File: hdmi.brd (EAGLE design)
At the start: 160 x 100 mm, 143 parts, among them IC1 FT2232HQ, U0 6SLX45CSG324, U1 MT41J64M16, U2 TPD12S016RKTR, U3 TPD12S016RKTR, U4 TPD12S016RKTR, U5 MNR18, U6 MNR18, U8 20Mhz

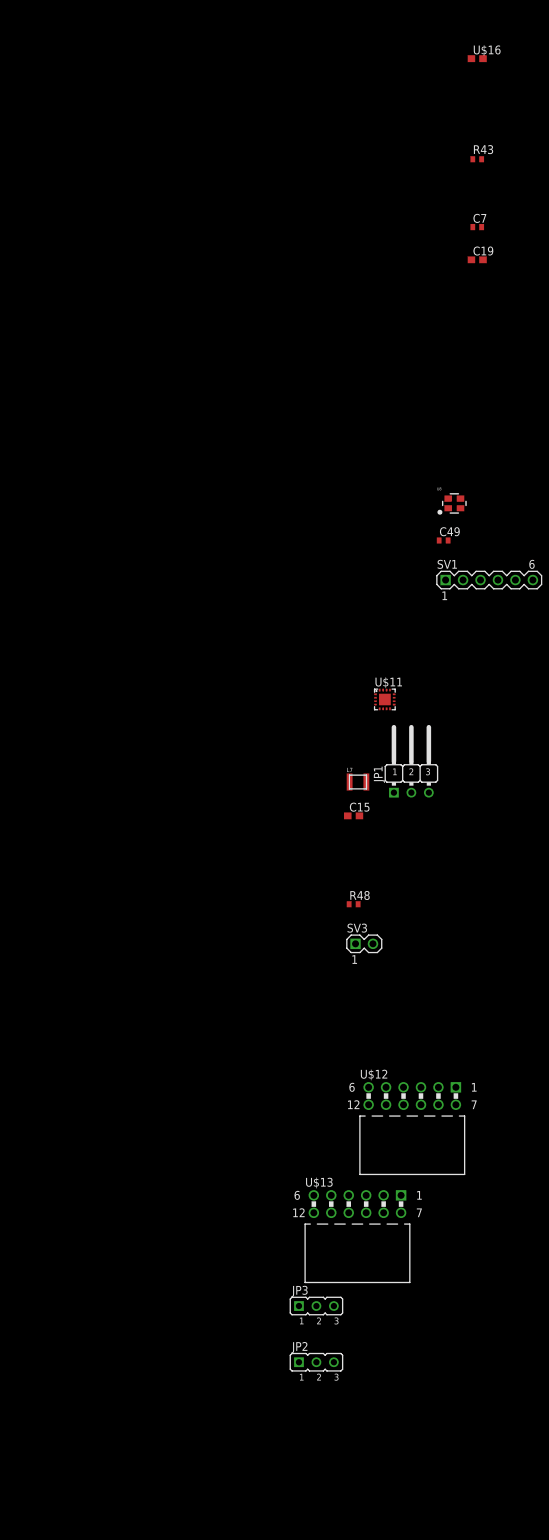
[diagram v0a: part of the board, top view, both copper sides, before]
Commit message: +Toslink
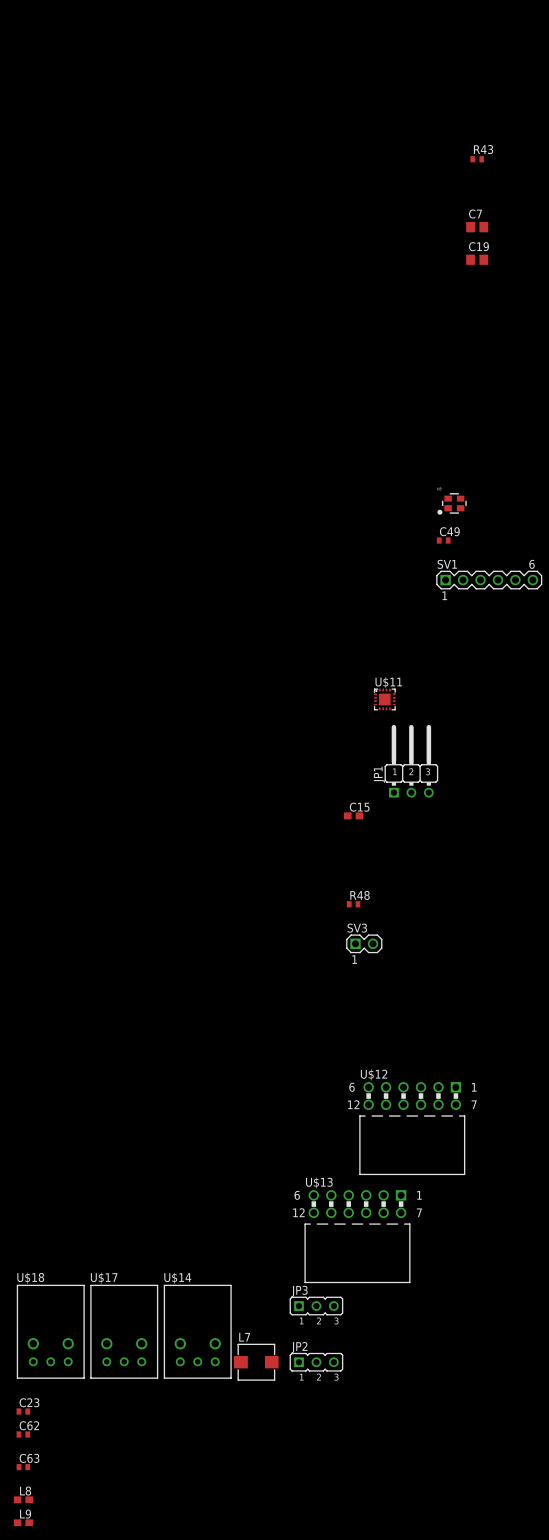
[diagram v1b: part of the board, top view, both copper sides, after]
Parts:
- removed U$16: 3A, prj-hdmi:0603
- added C23, C62, C63: 0.1u, prj-hdmi:0402
- added L8, L9: 47u, prj-hdmi:0603
- added U$14: PLT133-T10W, prj-hdmi:PLR135-T10_PLT133-T10W
- added U$17, U$18: PLR135-T10, prj-hdmi:PLR135-T10_PLT133-T10W
- C19: value 10u -> 47u; device prj-hdmi:0603 -> prj-hdmi:0805
- C7: value 10u -> 47u; device prj-hdmi:0402 -> prj-hdmi:0805
- L7: value 3.3u, 4A -> 3.3u, 5A; device prj-hdmi:1008 -> prj-hdmi:SRP5030T
- moved L7 85.7 mm to (-180.7, -914.0)
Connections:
- removed net N$29: C19.1, R48.2, U$11.11, U$11.2, U$11.3, U$16.2
- new net N$36: C23.1, L8.2, U$18.1
- new net N$4: C62.1, L9.2, U$17.1
- new net TOS_IN0: U$18.3
- new net TOS_IN1: U$17.3
- new net TOS_OUT0: U$14.3
- net +3V3: now also C57.1, C63.1, L8.1, L9.1, U$14.2; no longer C57.2
- net CENTER: now also C19.1, R48.2, U$11.11, U$11.2, U$11.3; no longer U$16.1
- net GND: now also C23.2, C57.2, C62.2, C63.2, U$14.1, U$17.2, U$18.2; no longer C57.1

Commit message: +Toslink connections
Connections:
- new net N$19: R48.1, U$11.8
- net TOS_IN0: now also U0.A2
- net TOS_IN1: now also U0.T18
- net TOS_OUT0: now also U0.V6
- net USB_5V_DISABLE: no longer R48.1, U$11.8
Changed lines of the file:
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@@
 <contactref element="U$10" pad="3"/>
 <contactref element="R44" pad="2"/>
-<contactref element="U$11" pad="8"/>
-<contactref element="R48" pad="1"/>
-<wire x1="-161.2766" y1="-818.9098" x2="-167.2232" y2="-847.344" width="0" layer="19" extent="1-1"/>
-<wire x1="-147.94" y1="-660.4" x2="-161.2766" y2="-818.9098" width="0" layer="19" extent="1-1"/>
 <wire x1="-148.59" y1="-655.1" x2="-147.94" y2="-660.4" width="0" layer="19" extent="1-1"/>
 </signal>
@@
 <signal name="TOS_IN0">
 <contactref element="U$18" pad="3"/>
+<contactref element="U0" pad="A2"/>
+<wire x1="-45.4" y1="16" x2="-213.1822" y2="-913.9312" width="0" layer="19" extent="1-1"/>
 </signal>
 <signal name="TOS_IN1">
 <contactref element="U$17" pad="3"/>
+<contactref element="U0" pad="T18"/>
+<wire x1="-32.6" y1="4" x2="-202.4888" y2="-913.9312" width="0" layer="19" extent="1-1"/>
 </signal>
 <signal name="TOS_OUT0">
 <contactref element="U$14" pad="3"/>
+<contactref element="U0" pad="V6"/>
+<wire x1="-42.2" y1="2.4" x2="-191.7954" y2="-913.9312" width="0" layer="19" extent="1-1"/>
+</signal>
+<signal name="N$19">
+<contactref element="U$11" pad="8"/>
+<contactref element="R48" pad="1"/>
+<wire x1="-161.2766" y1="-818.9098" x2="-167.2232" y2="-847.344" width="0" layer="19" extent="1-1"/>
 </signal>
 </signals>

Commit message: +Schematic notes
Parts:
- removed R48: 10k, prj-hdmi:0402
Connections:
- removed net N$19: R48.1, U$11.8
- net CENTER: no longer R48.2
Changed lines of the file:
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@@
 <layers>
 <layer number="1" name="Top" color="4" fill="1" visible="yes" active="yes"/>
-<layer number="2" name="Ground" color="1" fill="3" visible="no" active="no"/>
+<layer number="2" name="Ground" color="1" fill="3" visible="no" active="yes"/>
 <layer number="3" name="Route3" color="4" fill="3" visible="no" active="no"/>
 <layer number="4" name="Route4" color="1" fill="4" visible="no" active="no"/>
@@
 <layer number="13" name="Route13" color="4" fill="5" visible="no" active="no"/>
 <layer number="14" name="Route14" color="1" fill="6" visible="no" active="no"/>
-<layer number="15" name="VCC" color="4" fill="6" visible="no" active="no"/>
+<layer number="15" name="VCC" color="4" fill="6" visible="no" active="yes"/>
 <layer number="16" name="Bottom" color="1" fill="1" visible="yes" active="yes"/>
 <layer number="17" name="Pads" color="2" fill="1" visible="yes" active="yes"/>
@@
 </class>
 </classes>
-<designrules name="default">
+<designrules name="default *">
 <description language="de">&lt;b&gt;EAGLE Design Rules&lt;/b&gt;
 &lt;p&gt;
@@
 necessary adjustments and save your customized
 design rules under a new name.</description>
-<param name="layerSetup" value="(1*16)"/>
+<param name="layerSetup" value="(1*2+15*16)"/>
 <param name="mtCopper" value="0.035mm 0.035mm 0.035mm 0.035mm 0.035mm 0.035mm 0.035mm 0.035mm 0.035mm 0.035mm 0.035mm 0.035mm 0.035mm 0.035mm 0.035mm 0.035mm"/>
-<param name="mtIsolate" value="1.5mm 0.15mm 0.2mm 0.15mm 0.2mm 0.15mm 0.2mm 0.15mm 0.2mm 0.15mm 0.2mm 0.15mm 0.2mm 0.15mm 0.2mm"/>
+<param name="mtIsolate" value="5mil 40mil 0.2mm 0.15mm 0.2mm 0.15mm 0.2mm 0.15mm 0.2mm 0.15mm 0.2mm 0.15mm 0.2mm 0.15mm 5mil"/>
 <param name="mdWireWire" value="8mil"/>
 <param name="mdWirePad" value="8mil"/>
@@
 <element name="JP1" library="prj-hdmi" package="JP2W" value="5V_SEL" x="-158.1658" y="-829.8434"/>
 <element name="C15" library="prj-hdmi" package="0603" value="0.1u" x="-166.5732" y="-834.4916"/>
-<element name="R48" library="prj-hdmi" package="0402" value="10k" x="-166.5732" y="-847.344"/>
 <element name="SV3" library="prj-hdmi" package="MA02-1" value="EXT_SUP" x="-165.0238" y="-853.1098"/>
 <element name="U$12" library="prj-hdmi" package="PMOD-2X6" value="PMOD-2X6" x="-158.0388" y="-875.2586"/>
@@
 <contactref element="U$11" pad="3"/>
 <contactref element="U$11" pad="11"/>
-<contactref element="R48" pad="2"/>
 <contactref element="C19" pad="1"/>
-<wire x1="-166.2938" y1="-853.1098" x2="-165.9232" y2="-847.344" width="0" layer="19" extent="1-1"/>
-<wire x1="-163.3866" y1="-817.7998" x2="-165.9232" y2="-847.344" width="0" layer="19" extent="1-1"/>
-<wire x1="-163.3866" y1="-817.2998" x2="-163.3866" y2="-817.7998" width="0" layer="19" extent="1-1"/>
+<wire x1="-163.3866" y1="-817.7998" x2="-163.3866" y2="-817.2998" width="0" layer="19" extent="1-1"/>
 <wire x1="-160.6666" y1="-817.2998" x2="-163.3866" y2="-817.2998" width="0" layer="19" extent="1-1"/>
+<wire x1="-166.2938" y1="-853.1098" x2="-163.3866" y2="-817.7998" width="0" layer="19" extent="1-1"/>
 <wire x1="-149.54" y1="-753.5672" x2="-160.6666" y2="-817.2998" width="0" layer="19" extent="1-1"/>
 <wire x1="-135.8844" y1="-707.5424" x2="-149.54" y2="-753.5672" width="0" layer="19" extent="1-1"/>
@@
 <wire x1="-160.6666" y1="-817.7998" x2="-167.4232" y2="-834.4916" width="0" layer="19" extent="1-1"/>
 </signal>
-<signal name="SW@16">
+<signal name="SW@16" class="1">
 <contactref element="C15" pad="2"/>
 <contactref element="U$11" pad="1"/>
@@
 <wire x1="-182.971" y1="-913.9936" x2="-165.7232" y2="-834.4916" width="0" layer="19" extent="1-1"/>
 </signal>
-<signal name="N$30">
+<signal name="N$30" class="1">
 <contactref element="JP1" pad="1"/>
 <contactref element="U$11" pad="5"/>
@@
 <wire x1="-42.2" y1="2.4" x2="-191.7954" y2="-913.9312" width="0" layer="19" extent="1-1"/>
 </signal>
-<signal name="N$19">
-<contactref element="U$11" pad="8"/>
-<contactref element="R48" pad="1"/>
-<wire x1="-161.2766" y1="-818.9098" x2="-167.2232" y2="-847.344" width="0" layer="19" extent="1-1"/>
-</signal>
 </signals>

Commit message: Removed regulator for external power, schematics look good I think
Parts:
- removed L6: 1A, prj-hdmi:0603
- removed L7: 3.3u, 5A, prj-hdmi:SRP5030T
- removed U$11: MIC24085, prj-hdmi:QFN-16-3X3
- C15: value 0.1u -> 100u; device prj-hdmi:0603 -> rcl:C1206
- C19: value 47u -> 100u; device prj-hdmi:0805 -> rcl:C1206
- C7: value 47u -> 100u
- moved C19 205.8 mm to (-213.6, -948.8)
- moved C15 118.0 mm to (-213.6, -942.7)
- renumbered U$14 to TOSLINK_OUT0, U$15 to DC_JACK, U$17 to TOSLINK_IN1, U$18 to TOSLINK_IN0
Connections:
- removed net N$2: C15.1, U$11.10
- removed net N$30: JP1.1, L7.2, U$11.5
- removed net N$48: C7.1, L6.2, U$10.10, U$10.9
- removed net SW@16: C15.2, L7.1, U$11.1, U$11.12, U$11.13, U$11.16
- net +5V: now also C15.1
- net CENTER: now also JP1.1, SV3.2; no longer SV3.1, U$11.11, U$11.2, U$11.3
- net GND: now also C15.2, SV3.1; no longer SV3.2, U$11.14, U$11.15, U$11.4, U$11.ETP
- net N$45: now also C7.1, U$10.10, U$10.9; no longer L6.1

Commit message: +Bluetooth module
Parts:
- added C64, C65: 0.1, prj-hdmi:0402
- added R42, R47: 10k, prj-hdmi:0402
- added U$11: PAN1322, prj-hdmi:PAN1322
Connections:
- new net BT_CTS: U$11.F5, U0.V4
- new net BT_RESET#: R42.2, U$11.A3, U0.T5
- new net BT_RTS: U$11.F8, U0.T4
- new net BT_RX: U$11.E6, U0.T3
- new net BT_SCL: U$11.E2, U0.V5
- new net BT_SDA: U$11.E1, U0.U5
- new net BT_TX: U$11.F7, U0.R3
- new net BT_WAKE: R47.1, U$11.F4, U0.R5
- net +3V3: now also C64.1, C65.1, R47.2, U$11.A4, U$11.A5, U$11.A6, U$11.B5, U$11.C5, U$11.F6
- net GND: now also C64.2, C65.2, R42.1, U$11.A1, U$11.A11, U$11.A12, U$11.A7, U$11.A9, U$11.C8, U$11.C9, U$11.D7, U$11.D8, U$11.E8, U$11.E9, U$11.F1, U$11.F11, U$11.F12, U$11.F9
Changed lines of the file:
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@@
 <element name="C15" library="rcl" package="C1206" value="100u" x="-213.6394" y="-942.7464"/>
 <element name="C19" library="rcl" package="C1206" value="100u" x="-213.6394" y="-948.7662"/>
+<element name="U$11" library="prj-hdmi" package="PAN1322" value="PAN1322" x="-220.6244" y="-941.6796"/>
+<element name="C64" library="prj-hdmi" package="0402" value="0.1" x="-224.0788" y="-954.151"/>
+<element name="C65" library="prj-hdmi" package="0402" value="0.1" x="-224.0788" y="-957.5038"/>
+<element name="R42" library="prj-hdmi" package="0402" value="10k" x="-224.0788" y="-962.2536"/>
+<element name="R47" library="prj-hdmi" package="0402" value="10k" x="-224.0788" y="-967.0034"/>
 </elements>
 <signals>
@@
 <contactref element="C15" pad="2"/>
 <contactref element="C19" pad="2"/>
+<contactref element="U$11" pad="F12"/>
+<contactref element="U$11" pad="A1"/>
+<contactref element="U$11" pad="A7"/>
+<contactref element="U$11" pad="A9"/>
+<contactref element="U$11" pad="A12"/>
+<contactref element="U$11" pad="A11"/>
+<contactref element="U$11" pad="C8"/>
+<contactref element="U$11" pad="C9"/>
+<contactref element="U$11" pad="D7"/>
+<contactref element="U$11" pad="D8"/>
+<contactref element="U$11" pad="E8"/>
+<contactref element="U$11" pad="E9"/>
+<contactref element="U$11" pad="F1"/>
+<contactref element="U$11" pad="F11"/>
+<contactref element="U$11" pad="F9"/>
+<contactref element="C64" pad="2"/>
+<contactref element="C65" pad="2"/>
+<contactref element="R42" pad="1"/>
 <wire x1="-88.25" y1="-161.29" x2="-88.25" y2="-166.37" width="0" layer="19" extent="1-1"/>
 <wire x1="-88.25" y1="-171.45" x2="-88.25" y2="-166.37" width="0" layer="19" extent="1-1"/>
@@
 <wire x1="-213.98" y1="-924.5092" x2="-213.98" y2="-921.1564" width="0" layer="19" extent="1-1"/>
 <wire x1="-213.98" y1="-929.259" x2="-213.98" y2="-924.5092" width="0" layer="19" extent="1-1"/>
-<wire x1="-212.2394" y1="-942.7464" x2="-213.98" y2="-929.259" width="0" layer="19" extent="1-1"/>
+<wire x1="-217.7194" y1="-935.0996" x2="-213.98" y2="-929.259" width="0" layer="19" extent="1-1"/>
+<wire x1="-217.7194" y1="-936.2996" x2="-217.7194" y2="-935.0996" width="0" layer="19" extent="1-1"/>
+<wire x1="-217.7194" y1="-938.6996" x2="-217.7194" y2="-936.2996" width="0" layer="19" extent="1-1"/>
+<wire x1="-217.7194" y1="-941.0996" x2="-217.7194" y2="-938.6996" width="0" layer="19" extent="1-1"/>
+<wire x1="-220.1194" y1="-938.6496" x2="-217.7194" y2="-938.6996" width="0" layer="19" extent="1-1"/>
+<wire x1="-220.1194" y1="-939.8496" x2="-220.1194" y2="-938.6496" width="0" layer="19" extent="1-1"/>
+<wire x1="-221.3194" y1="-939.8996" x2="-220.1194" y2="-939.8496" width="0" layer="19" extent="1-1"/>
+<wire x1="-221.3194" y1="-941.0996" x2="-221.3194" y2="-939.8996" width="0" layer="19" extent="1-1"/>
+<wire x1="-222.5194" y1="-939.8996" x2="-221.3194" y2="-939.8996" width="0" layer="19" extent="1-1"/>
+<wire x1="-222.5194" y1="-938.6996" x2="-222.5194" y2="-939.8996" width="0" layer="19" extent="1-1"/>
+<wire x1="-223.7194" y1="-938.6996" x2="-222.5194" y2="-938.6996" width="0" layer="19" extent="1-1"/>
+<wire x1="-223.7194" y1="-936.2996" x2="-223.7194" y2="-938.6996" width="0" layer="19" extent="1-1"/>
+<wire x1="-223.7194" y1="-935.0996" x2="-223.7194" y2="-936.2996" width="0" layer="19" extent="1-1"/>
+<wire x1="-212.2394" y1="-942.7464" x2="-217.7194" y2="-941.0996" width="0" layer="19" extent="1-1"/>
 <wire x1="-212.2394" y1="-948.7662" x2="-212.2394" y2="-942.7464" width="0" layer="19" extent="1-1"/>
+<wire x1="-217.7194" y1="-948.2996" x2="-212.2394" y2="-948.7662" width="0" layer="19" extent="1-1"/>
+<wire x1="-223.7194" y1="-948.2996" x2="-217.7194" y2="-948.2996" width="0" layer="19" extent="1-1"/>
+<wire x1="-223.4288" y1="-954.151" x2="-223.7194" y2="-948.2996" width="0" layer="19" extent="1-1"/>
+<wire x1="-223.4288" y1="-957.5038" x2="-223.4288" y2="-954.151" width="0" layer="19" extent="1-1"/>
+<wire x1="-224.7288" y1="-962.2536" x2="-223.4288" y2="-957.5038" width="0" layer="19" extent="1-1"/>
 </signal>
 <signal name="+3V3" class="1">
@@
 <contactref element="L8" pad="1"/>
 <contactref element="L9" pad="1"/>
+<contactref element="U$11" pad="B5"/>
+<contactref element="U$11" pad="F6"/>
+<contactref element="U$11" pad="C5"/>
+<contactref element="U$11" pad="A4"/>
+<contactref element="C64" pad="1"/>
+<contactref element="C65" pad="1"/>
+<contactref element="U$11" pad="A5"/>
+<contactref element="U$11" pad="A6"/>
+<contactref element="R47" pad="2"/>
 <wire x1="-142.86" y1="-609.6" x2="-142.86" y2="-614.68" width="0" layer="19" extent="1-1"/>
 <wire x1="-142.86" y1="-604.52" x2="-142.86" y2="-609.6" width="0" layer="19" extent="1-1"/>
@@
 <wire x1="-215.48" y1="-934.0088" x2="-215.28" y2="-929.259" width="0" layer="19" extent="1-1"/>
 <wire x1="-215.48" y1="-937.3616" x2="-215.48" y2="-934.0088" width="0" layer="19" extent="1-1"/>
+<wire x1="-217.7194" y1="-942.2996" x2="-215.48" y2="-937.3616" width="0" layer="19" extent="1-1"/>
+<wire x1="-217.7194" y1="-943.4996" x2="-217.7194" y2="-942.2996" width="0" layer="19" extent="1-1"/>
+<wire x1="-218.9194" y1="-943.4996" x2="-217.7194" y2="-943.4996" width="0" layer="19" extent="1-1"/>
+<wire x1="-220.1194" y1="-943.4496" x2="-218.9194" y2="-943.4996" width="0" layer="19" extent="1-1"/>
+<wire x1="-217.7194" y1="-944.6996" x2="-217.7194" y2="-943.4996" width="0" layer="19" extent="1-1"/>
+<wire x1="-223.7194" y1="-942.2996" x2="-220.1194" y2="-943.4496" width="0" layer="19" extent="1-1"/>
+<wire x1="-224.7288" y1="-954.151" x2="-220.1194" y2="-943.4496" width="0" layer="19" extent="1-1"/>
+<wire x1="-224.7288" y1="-957.5038" x2="-224.7288" y2="-954.151" width="0" layer="19" extent="1-1"/>
+<wire x1="-223.4288" y1="-967.0034" x2="-224.7288" y2="-957.5038" width="0" layer="19" extent="1-1"/>
 <wire x1="-43.8" y1="3.2" x2="-56.53" y2="-107.95" width="0" layer="19" extent="1-1"/>
 <wire x1="-42.2" y1="4.8" x2="-43.8" y2="3.2" width="0" layer="19" extent="1-1"/>
@@
 <wire x1="-135.8844" y1="-707.5424" x2="-160.7058" y2="-831.1134" width="0" layer="19" extent="1-1"/>
 </signal>
+<signal name="BT_RESET#">
+<contactref element="R42" pad="2"/>
+<contactref element="U$11" pad="A3"/>
+<contactref element="U0" pad="T5"/>
+<wire x1="-217.7194" y1="-945.8996" x2="-223.4288" y2="-962.2536" width="0" layer="19" extent="1-1"/>
+<wire x1="-43" y1="4" x2="-223.4288" y2="-962.2536" width="0" layer="19" extent="1-1"/>
+</signal>
+<signal name="BT_TX">
+<contactref element="U$11" pad="F7"/>
+<contactref element="U0" pad="R3"/>
+<wire x1="-44.6" y1="4.8" x2="-223.7194" y2="-941.0996" width="0" layer="19" extent="1-1"/>
+</signal>
+<signal name="BT_RX">
+<contactref element="U$11" pad="E6"/>
+<contactref element="U0" pad="T3"/>
+<wire x1="-44.6" y1="4" x2="-222.5194" y2="-942.2996" width="0" layer="19" extent="1-1"/>
+</signal>
+<signal name="BT_RTS">
+<contactref element="U$11" pad="F8"/>
+<contactref element="U0" pad="T4"/>
+<wire x1="-43.8" y1="4" x2="-223.7194" y2="-939.8996" width="0" layer="19" extent="1-1"/>
+</signal>
+<signal name="BT_CTS">
+<contactref element="U$11" pad="F5"/>
+<contactref element="U0" pad="V4"/>
+<wire x1="-43.8" y1="2.4" x2="-223.7194" y2="-943.4996" width="0" layer="19" extent="1-1"/>
+</signal>
+<signal name="BT_SDA">
+<contactref element="U$11" pad="E1"/>
+<contactref element="U0" pad="U5"/>
+<wire x1="-43" y1="3.2" x2="-222.5194" y2="-948.2996" width="0" layer="19" extent="1-1"/>
+</signal>
+<signal name="BT_SCL">
+<contactref element="U$11" pad="E2"/>
+<contactref element="U0" pad="V5"/>
+<wire x1="-43" y1="2.4" x2="-222.5194" y2="-947.0996" width="0" layer="19" extent="1-1"/>
+</signal>
+<signal name="BT_WAKE">
+<contactref element="U$11" pad="F4"/>
+<contactref element="R47" pad="1"/>
+<contactref element="U0" pad="R5"/>
+<wire x1="-223.7194" y1="-944.6996" x2="-224.7288" y2="-967.0034" width="0" layer="19" extent="1-1"/>
+<wire x1="-43" y1="4.8" x2="-224.7288" y2="-967.0034" width="0" layer="19" extent="1-1"/>
+</signal>
 </signals>

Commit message: Began moving components in the board layout
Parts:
- JP1: device prj-hdmi:JP2W -> prj-hdmi:JP2
- U$10: device Texas Instruments:SON10 -> prj-hdmi:SON10
- moved R47 1097.0 mm to (-31.8, 113.0)
- moved R42 1093.3 mm to (-26.7, 113.0)
- moved C65 1089.5 mm to (-21.6, 113.0)
- moved C64 1087.2 mm to (-16.5, 113.0)
- moved L9 1064.5 mm to (-41.9, 113.0)
- moved L8 1062.0 mm to (-36.8, 113.0)
- moved C63 1045.0 mm to (-87.6, 108.0)
- moved C62 1040.9 mm to (-82.5, 108.0)
- moved C23 1031.3 mm to (-92.7, 102.9)
- moved C19 1030.5 mm to (-85.1, 73.7)
- moved C15 1025.3 mm to (-78.7, 73.7)
- moved JP2 986.2 mm to (-50.8, 64.8)
- moved JP3 975.9 mm to (-69.8, 64.8)
- moved SV3 963.6 mm to (19.0, 92.8), turned to 270 degrees
- moved U$11 959.3 mm to (-101.6, 10.2)
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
